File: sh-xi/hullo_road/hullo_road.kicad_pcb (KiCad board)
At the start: 2 copper layers, 70 x 43.5 mm, 139 parts

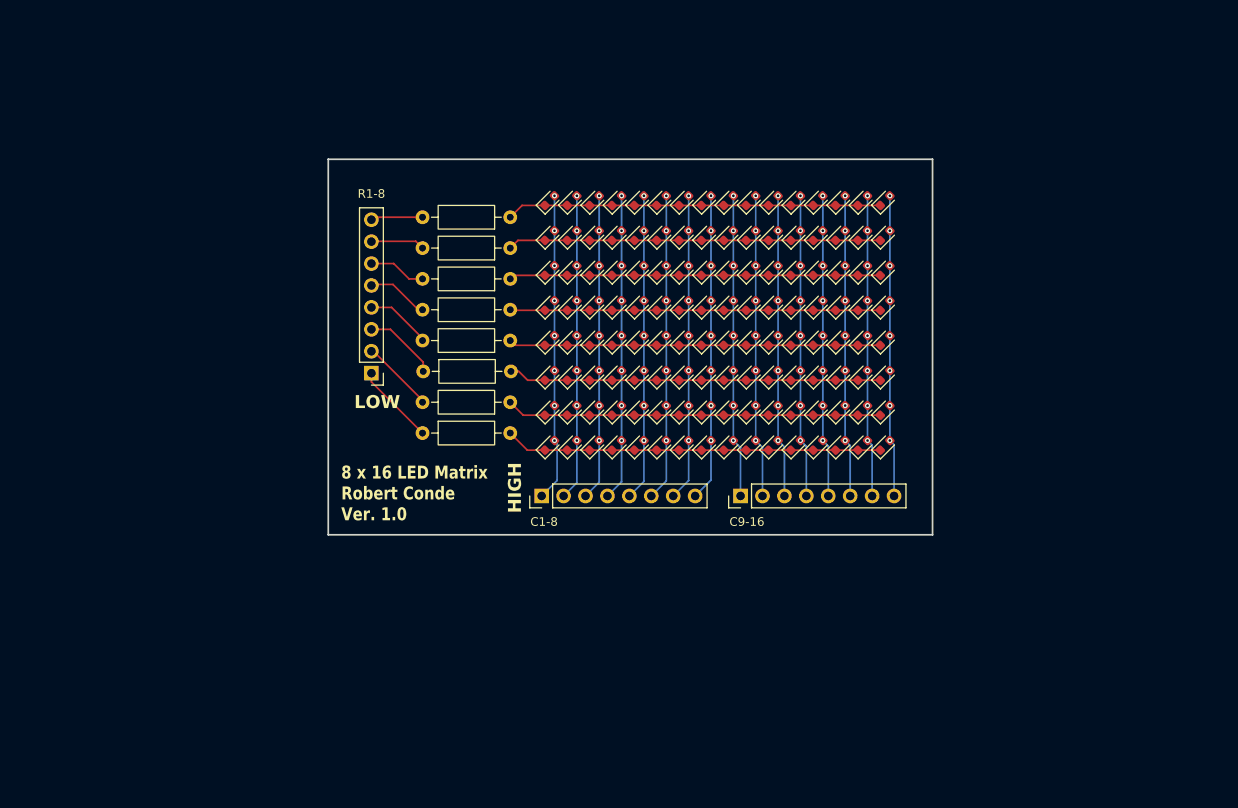
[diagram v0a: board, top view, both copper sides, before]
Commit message: Add LED matrix
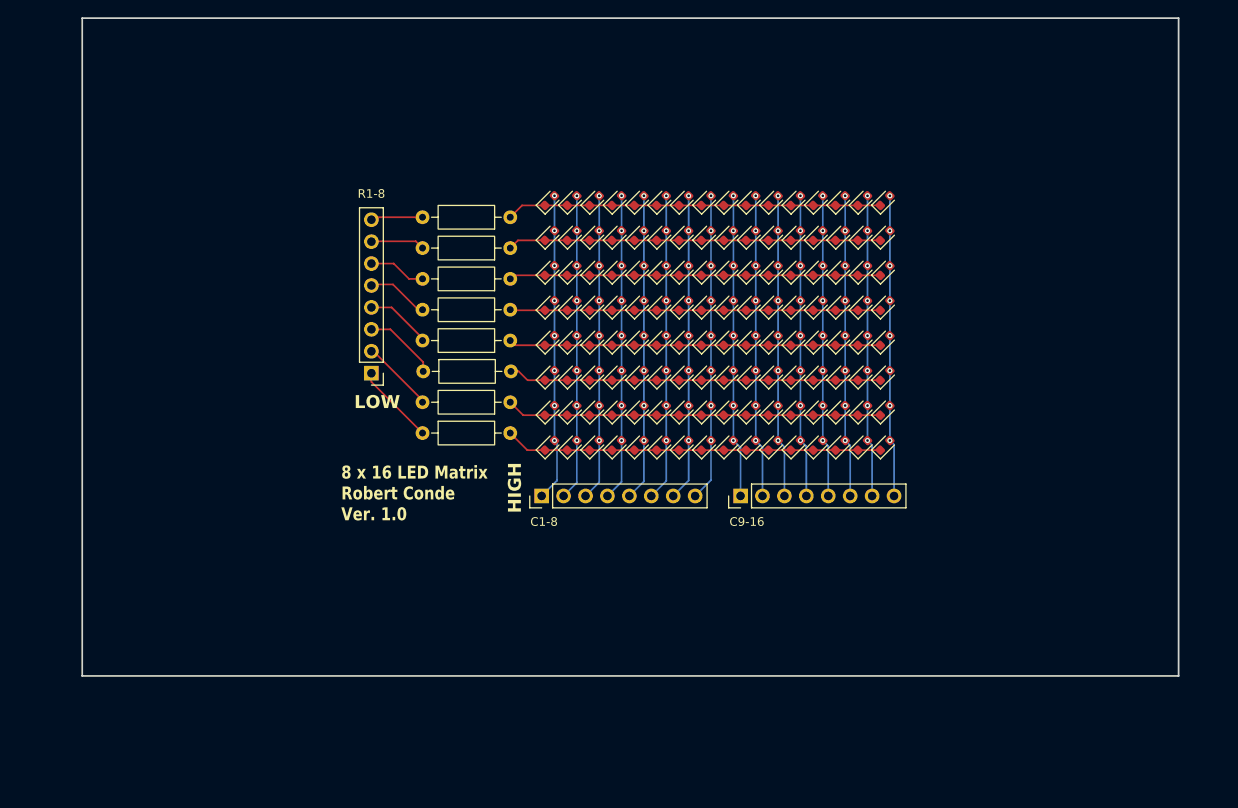
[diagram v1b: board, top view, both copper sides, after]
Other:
- board size 70 x 43.5 mm -> 127 x 76.2 mm
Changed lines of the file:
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@@
 	)
 	(gr_rect
-		(start 59.5 86)
-		(end 129.5 129.5)
+		(start 31 69.65)
+		(end 158 145.85)
 		(stroke
 			(width 0.2)
-			(type default)
+			(type solid)
 		)
 		(fill no)
+		(locked yes)
 		(layer "Edge.Cuts")
 	)

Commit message: Place LEDs in a grid
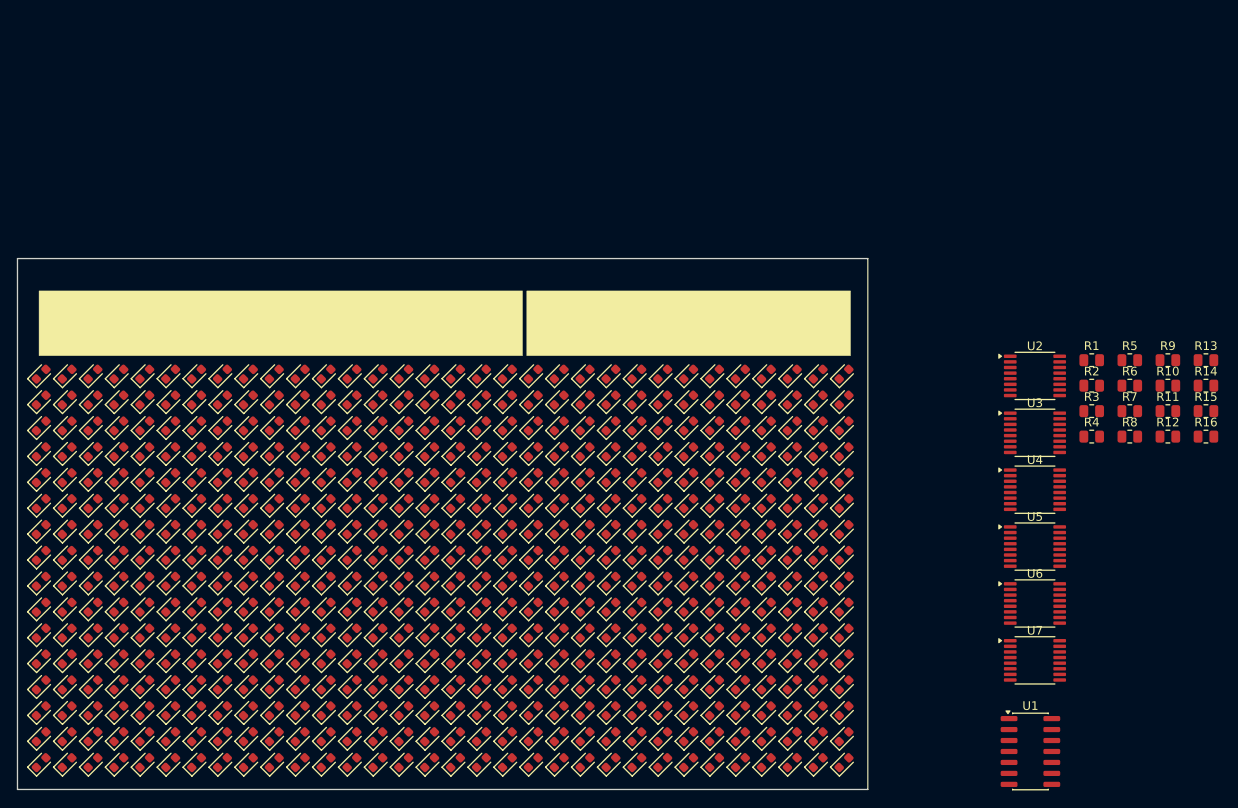
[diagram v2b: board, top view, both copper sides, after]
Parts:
- removed C1-8, C9-16, R1-8: Conn_01x08, Connector_PinHeader_2.54mm:PinHeader_1x08_P2.54mm_Vertical
- added D129: LED, LED_SMD:LED_0603_1608Metric, F.Cu at (26.2, 122.9)
- added D130: LED, LED_SMD:LED_0603_1608Metric, F.Cu at (29.2, 122.9)
- added D131: LED, LED_SMD:LED_0603_1608Metric, F.Cu at (32.2, 122.9)
- added D132: LED, LED_SMD:LED_0603_1608Metric, F.Cu at (35.2, 122.9)
- added D133: LED, LED_SMD:LED_0603_1608Metric, F.Cu at (38.2, 122.9)
- added D134: LED, LED_SMD:LED_0603_1608Metric, F.Cu at (41.2, 122.9)
- added D135: LED, LED_SMD:LED_0603_1608Metric, F.Cu at (44.2, 122.9)
- added D136: LED, LED_SMD:LED_0603_1608Metric, F.Cu at (47.2, 122.9)
- added D137: LED, LED_SMD:LED_0603_1608Metric, F.Cu at (50.2, 122.9)
- added D138: LED, LED_SMD:LED_0603_1608Metric, F.Cu at (53.2, 122.9)
- added D139: LED, LED_SMD:LED_0603_1608Metric, F.Cu at (56.2, 122.9)
- added D140: LED, LED_SMD:LED_0603_1608Metric, F.Cu at (59.2, 122.9)
- added D141: LED, LED_SMD:LED_0603_1608Metric, F.Cu at (62.2, 122.9)
- added D142: LED, LED_SMD:LED_0603_1608Metric, F.Cu at (65.2, 122.9)
- added D143: LED, LED_SMD:LED_0603_1608Metric, F.Cu at (68.2, 122.9)
- added D144: LED, LED_SMD:LED_0603_1608Metric, F.Cu at (71.2, 122.9)
- added D145: LED, LED_SMD:LED_0603_1608Metric, F.Cu at (74.2, 122.9)
- added D146: LED, LED_SMD:LED_0603_1608Metric, F.Cu at (77.2, 122.9)
- added D147: LED, LED_SMD:LED_0603_1608Metric, F.Cu at (80.2, 122.9)
- added D148: LED, LED_SMD:LED_0603_1608Metric, F.Cu at (83.2, 122.9)
- added D149: LED, LED_SMD:LED_0603_1608Metric, F.Cu at (86.2, 122.9)
- added D150: LED, LED_SMD:LED_0603_1608Metric, F.Cu at (89.2, 122.9)
- added D151: LED, LED_SMD:LED_0603_1608Metric, F.Cu at (92.2, 122.9)
- added D152: LED, LED_SMD:LED_0603_1608Metric, F.Cu at (95.2, 122.9)
- added D153: LED, LED_SMD:LED_0603_1608Metric, F.Cu at (98.2, 122.9)
- added D154: LED, LED_SMD:LED_0603_1608Metric, F.Cu at (101.2, 122.9)
- added D155: LED, LED_SMD:LED_0603_1608Metric, F.Cu at (104.2, 122.9)
- added D156: LED, LED_SMD:LED_0603_1608Metric, F.Cu at (107.2, 122.9)
- added D157: LED, LED_SMD:LED_0603_1608Metric, F.Cu at (110.2, 122.9)
- added D158: LED, LED_SMD:LED_0603_1608Metric, F.Cu at (113.2, 122.9)
- added D159: LED, LED_SMD:LED_0603_1608Metric, F.Cu at (116.2, 122.9)
- added D160: LED, LED_SMD:LED_0603_1608Metric, F.Cu at (119.2, 122.9)
- added D161: LED, LED_SMD:LED_0603_1608Metric, F.Cu at (26.2, 125.9)
- added D162: LED, LED_SMD:LED_0603_1608Metric, F.Cu at (29.2, 125.9)
- added D163: LED, LED_SMD:LED_0603_1608Metric, F.Cu at (32.2, 125.9)
- added D164: LED, LED_SMD:LED_0603_1608Metric, F.Cu at (35.2, 125.9)
- added D165: LED, LED_SMD:LED_0603_1608Metric, F.Cu at (38.2, 125.9)
- added D166: LED, LED_SMD:LED_0603_1608Metric, F.Cu at (41.2, 125.9)
- added D167: LED, LED_SMD:LED_0603_1608Metric, F.Cu at (44.2, 125.9)
- added D168: LED, LED_SMD:LED_0603_1608Metric, F.Cu at (47.2, 125.9)
- added D169: LED, LED_SMD:LED_0603_1608Metric, F.Cu at (50.2, 125.9)
- added D170: LED, LED_SMD:LED_0603_1608Metric, F.Cu at (53.2, 125.9)
- added D171: LED, LED_SMD:LED_0603_1608Metric, F.Cu at (56.2, 125.9)
- added D172: LED, LED_SMD:LED_0603_1608Metric, F.Cu at (59.2, 125.9)
- added D173: LED, LED_SMD:LED_0603_1608Metric, F.Cu at (62.2, 125.9)
- added D174: LED, LED_SMD:LED_0603_1608Metric, F.Cu at (65.2, 125.9)
- added D175: LED, LED_SMD:LED_0603_1608Metric, F.Cu at (68.2, 125.9)
- added D176: LED, LED_SMD:LED_0603_1608Metric, F.Cu at (71.2, 125.9)
- added D177: LED, LED_SMD:LED_0603_1608Metric, F.Cu at (74.2, 125.9)
- added D178: LED, LED_SMD:LED_0603_1608Metric, F.Cu at (77.2, 125.9)
- added D179: LED, LED_SMD:LED_0603_1608Metric, F.Cu at (80.2, 125.9)
- added D180: LED, LED_SMD:LED_0603_1608Metric, F.Cu at (83.2, 125.9)
- added D181: LED, LED_SMD:LED_0603_1608Metric, F.Cu at (86.2, 125.9)
- added D182: LED, LED_SMD:LED_0603_1608Metric, F.Cu at (89.2, 125.9)
- added D183: LED, LED_SMD:LED_0603_1608Metric, F.Cu at (92.2, 125.9)
- added D184: LED, LED_SMD:LED_0603_1608Metric, F.Cu at (95.2, 125.9)
- added D185: LED, LED_SMD:LED_0603_1608Metric, F.Cu at (98.2, 125.9)
- added D186: LED, LED_SMD:LED_0603_1608Metric, F.Cu at (101.2, 125.9)
- added D187: LED, LED_SMD:LED_0603_1608Metric, F.Cu at (104.2, 125.9)
- added D188: LED, LED_SMD:LED_0603_1608Metric, F.Cu at (107.2, 125.9)
- added D189: LED, LED_SMD:LED_0603_1608Metric, F.Cu at (110.2, 125.9)
- added D190: LED, LED_SMD:LED_0603_1608Metric, F.Cu at (113.2, 125.9)
- added D191: LED, LED_SMD:LED_0603_1608Metric, F.Cu at (116.2, 125.9)
- added D192: LED, LED_SMD:LED_0603_1608Metric, F.Cu at (119.2, 125.9)
- added D193: LED, LED_SMD:LED_0603_1608Metric, F.Cu at (26.2, 128.9)
- added D194: LED, LED_SMD:LED_0603_1608Metric, F.Cu at (29.2, 128.9)
- added D195: LED, LED_SMD:LED_0603_1608Metric, F.Cu at (32.2, 128.9)
- added D196: LED, LED_SMD:LED_0603_1608Metric, F.Cu at (35.2, 128.9)
- added D197: LED, LED_SMD:LED_0603_1608Metric, F.Cu at (38.2, 128.9)
- added D198: LED, LED_SMD:LED_0603_1608Metric, F.Cu at (41.2, 128.9)
- added D199: LED, LED_SMD:LED_0603_1608Metric, F.Cu at (44.2, 128.9)
- added D200: LED, LED_SMD:LED_0603_1608Metric, F.Cu at (47.2, 128.9)
- added D201: LED, LED_SMD:LED_0603_1608Metric, F.Cu at (50.2, 128.9)
- added D202: LED, LED_SMD:LED_0603_1608Metric, F.Cu at (53.2, 128.9)
- added D203: LED, LED_SMD:LED_0603_1608Metric, F.Cu at (56.2, 128.9)
- added D204: LED, LED_SMD:LED_0603_1608Metric, F.Cu at (59.2, 128.9)
- added D205: LED, LED_SMD:LED_0603_1608Metric, F.Cu at (62.2, 128.9)
- added D206: LED, LED_SMD:LED_0603_1608Metric, F.Cu at (65.2, 128.9)
- added D207: LED, LED_SMD:LED_0603_1608Metric, F.Cu at (68.2, 128.9)
- added D208: LED, LED_SMD:LED_0603_1608Metric, F.Cu at (71.2, 128.9)
- added D209: LED, LED_SMD:LED_0603_1608Metric, F.Cu at (74.2, 128.9)
- added D210: LED, LED_SMD:LED_0603_1608Metric, F.Cu at (77.2, 128.9)
- added D211: LED, LED_SMD:LED_0603_1608Metric, F.Cu at (80.2, 128.9)
- added D212: LED, LED_SMD:LED_0603_1608Metric, F.Cu at (83.2, 128.9)
- added D213: LED, LED_SMD:LED_0603_1608Metric, F.Cu at (86.2, 128.9)
- added D214: LED, LED_SMD:LED_0603_1608Metric, F.Cu at (89.2, 128.9)
- added D215: LED, LED_SMD:LED_0603_1608Metric, F.Cu at (92.2, 128.9)
- added D216: LED, LED_SMD:LED_0603_1608Metric, F.Cu at (95.2, 128.9)
- added D217: LED, LED_SMD:LED_0603_1608Metric, F.Cu at (98.2, 128.9)
- added D218: LED, LED_SMD:LED_0603_1608Metric, F.Cu at (101.2, 128.9)
- added D219: LED, LED_SMD:LED_0603_1608Metric, F.Cu at (104.2, 128.9)
- added D220: LED, LED_SMD:LED_0603_1608Metric, F.Cu at (107.2, 128.9)
- added D221: LED, LED_SMD:LED_0603_1608Metric, F.Cu at (110.2, 128.9)
- added D222: LED, LED_SMD:LED_0603_1608Metric, F.Cu at (113.2, 128.9)
- added D223: LED, LED_SMD:LED_0603_1608Metric, F.Cu at (116.2, 128.9)
- added D224: LED, LED_SMD:LED_0603_1608Metric, F.Cu at (119.2, 128.9)
- added D225: LED, LED_SMD:LED_0603_1608Metric, F.Cu at (26.2, 131.9)
- added D226: LED, LED_SMD:LED_0603_1608Metric, F.Cu at (29.2, 131.9)
- added D227: LED, LED_SMD:LED_0603_1608Metric, F.Cu at (32.2, 131.9)
- added D228: LED, LED_SMD:LED_0603_1608Metric, F.Cu at (35.2, 131.9)
- added D229: LED, LED_SMD:LED_0603_1608Metric, F.Cu at (38.2, 131.9)
- added D230: LED, LED_SMD:LED_0603_1608Metric, F.Cu at (41.2, 131.9)
- added D231: LED, LED_SMD:LED_0603_1608Metric, F.Cu at (44.2, 131.9)
- added D232: LED, LED_SMD:LED_0603_1608Metric, F.Cu at (47.2, 131.9)
- added D233: LED, LED_SMD:LED_0603_1608Metric, F.Cu at (50.2, 131.9)
- added D234: LED, LED_SMD:LED_0603_1608Metric, F.Cu at (53.2, 131.9)
- added D235: LED, LED_SMD:LED_0603_1608Metric, F.Cu at (56.2, 131.9)
- added D236: LED, LED_SMD:LED_0603_1608Metric, F.Cu at (59.2, 131.9)
- added D237: LED, LED_SMD:LED_0603_1608Metric, F.Cu at (62.2, 131.9)
- added D238: LED, LED_SMD:LED_0603_1608Metric, F.Cu at (65.2, 131.9)
- added D239: LED, LED_SMD:LED_0603_1608Metric, F.Cu at (68.2, 131.9)
- added D240: LED, LED_SMD:LED_0603_1608Metric, F.Cu at (71.2, 131.9)
- added D241: LED, LED_SMD:LED_0603_1608Metric, F.Cu at (74.2, 131.9)
- added D242: LED, LED_SMD:LED_0603_1608Metric, F.Cu at (77.2, 131.9)
- added D243: LED, LED_SMD:LED_0603_1608Metric, F.Cu at (80.2, 131.9)
- added D244: LED, LED_SMD:LED_0603_1608Metric, F.Cu at (83.2, 131.9)
- added D245: LED, LED_SMD:LED_0603_1608Metric, F.Cu at (86.2, 131.9)
- added D246: LED, LED_SMD:LED_0603_1608Metric, F.Cu at (89.2, 131.9)
- added D247: LED, LED_SMD:LED_0603_1608Metric, F.Cu at (92.2, 131.9)
- added D248: LED, LED_SMD:LED_0603_1608Metric, F.Cu at (95.2, 131.9)
- added D249: LED, LED_SMD:LED_0603_1608Metric, F.Cu at (98.2, 131.9)
- added D250: LED, LED_SMD:LED_0603_1608Metric, F.Cu at (101.2, 131.9)
- added D251: LED, LED_SMD:LED_0603_1608Metric, F.Cu at (104.2, 131.9)
- added D252: LED, LED_SMD:LED_0603_1608Metric, F.Cu at (107.2, 131.9)
- added D253: LED, LED_SMD:LED_0603_1608Metric, F.Cu at (110.2, 131.9)
- added D254: LED, LED_SMD:LED_0603_1608Metric, F.Cu at (113.2, 131.9)
- added D255: LED, LED_SMD:LED_0603_1608Metric, F.Cu at (116.2, 131.9)
- added D256: LED, LED_SMD:LED_0603_1608Metric, F.Cu at (119.2, 131.9)
- added D257: LED, LED_SMD:LED_0603_1608Metric, F.Cu at (26.2, 134.9)
- added D258: LED, LED_SMD:LED_0603_1608Metric, F.Cu at (29.2, 134.9)
- added D259: LED, LED_SMD:LED_0603_1608Metric, F.Cu at (32.2, 134.9)
- added D260: LED, LED_SMD:LED_0603_1608Metric, F.Cu at (35.2, 134.9)
- added D261: LED, LED_SMD:LED_0603_1608Metric, F.Cu at (38.2, 134.9)
- added D262: LED, LED_SMD:LED_0603_1608Metric, F.Cu at (41.2, 134.9)
- added D263: LED, LED_SMD:LED_0603_1608Metric, F.Cu at (44.2, 134.9)
- added D264: LED, LED_SMD:LED_0603_1608Metric, F.Cu at (47.2, 134.9)
- added D265: LED, LED_SMD:LED_0603_1608Metric, F.Cu at (50.2, 134.9)
- added D266: LED, LED_SMD:LED_0603_1608Metric, F.Cu at (53.2, 134.9)
- added D267: LED, LED_SMD:LED_0603_1608Metric, F.Cu at (56.2, 134.9)
- added D268: LED, LED_SMD:LED_0603_1608Metric, F.Cu at (59.2, 134.9)
- added D269: LED, LED_SMD:LED_0603_1608Metric, F.Cu at (62.2, 134.9)
- added D270: LED, LED_SMD:LED_0603_1608Metric, F.Cu at (65.2, 134.9)
- added D271: LED, LED_SMD:LED_0603_1608Metric, F.Cu at (68.2, 134.9)
- added D272: LED, LED_SMD:LED_0603_1608Metric, F.Cu at (71.2, 134.9)
- added D273: LED, LED_SMD:LED_0603_1608Metric, F.Cu at (74.2, 134.9)
- added D274: LED, LED_SMD:LED_0603_1608Metric, F.Cu at (77.2, 134.9)
- added D275: LED, LED_SMD:LED_0603_1608Metric, F.Cu at (80.2, 134.9)
- added D276: LED, LED_SMD:LED_0603_1608Metric, F.Cu at (83.2, 134.9)
- added D277: LED, LED_SMD:LED_0603_1608Metric, F.Cu at (86.2, 134.9)
- added D278: LED, LED_SMD:LED_0603_1608Metric, F.Cu at (89.2, 134.9)
- added D279: LED, LED_SMD:LED_0603_1608Metric, F.Cu at (92.2, 134.9)
- added D280: LED, LED_SMD:LED_0603_1608Metric, F.Cu at (95.2, 134.9)
- added D281: LED, LED_SMD:LED_0603_1608Metric, F.Cu at (98.2, 134.9)
- added D282: LED, LED_SMD:LED_0603_1608Metric, F.Cu at (101.2, 134.9)
- added D283: LED, LED_SMD:LED_0603_1608Metric, F.Cu at (104.2, 134.9)
- added D284: LED, LED_SMD:LED_0603_1608Metric, F.Cu at (107.2, 134.9)
- added D285: LED, LED_SMD:LED_0603_1608Metric, F.Cu at (110.2, 134.9)
- added D286: LED, LED_SMD:LED_0603_1608Metric, F.Cu at (113.2, 134.9)
- added D287: LED, LED_SMD:LED_0603_1608Metric, F.Cu at (116.2, 134.9)
- added D288: LED, LED_SMD:LED_0603_1608Metric, F.Cu at (119.2, 134.9)
- added D289: LED, LED_SMD:LED_0603_1608Metric, F.Cu at (26.2, 137.9)
- added D290: LED, LED_SMD:LED_0603_1608Metric, F.Cu at (29.2, 137.9)
- added D291: LED, LED_SMD:LED_0603_1608Metric, F.Cu at (32.2, 137.9)
- added D292: LED, LED_SMD:LED_0603_1608Metric, F.Cu at (35.2, 137.9)
- added D293: LED, LED_SMD:LED_0603_1608Metric, F.Cu at (38.2, 137.9)
- added D294: LED, LED_SMD:LED_0603_1608Metric, F.Cu at (41.2, 137.9)
- added D295: LED, LED_SMD:LED_0603_1608Metric, F.Cu at (44.2, 137.9)
- added D296: LED, LED_SMD:LED_0603_1608Metric, F.Cu at (47.2, 137.9)
- added D297: LED, LED_SMD:LED_0603_1608Metric, F.Cu at (50.2, 137.9)
- added D298: LED, LED_SMD:LED_0603_1608Metric, F.Cu at (53.2, 137.9)
- added D299: LED, LED_SMD:LED_0603_1608Metric, F.Cu at (56.2, 137.9)
- added D300: LED, LED_SMD:LED_0603_1608Metric, F.Cu at (59.2, 137.9)
- added D301: LED, LED_SMD:LED_0603_1608Metric, F.Cu at (62.2, 137.9)
- added D302: LED, LED_SMD:LED_0603_1608Metric, F.Cu at (65.2, 137.9)
- added D303: LED, LED_SMD:LED_0603_1608Metric, F.Cu at (68.2, 137.9)
- added D304: LED, LED_SMD:LED_0603_1608Metric, F.Cu at (71.2, 137.9)
- added D305: LED, LED_SMD:LED_0603_1608Metric, F.Cu at (74.2, 137.9)
- added D306: LED, LED_SMD:LED_0603_1608Metric, F.Cu at (77.2, 137.9)
- added D307: LED, LED_SMD:LED_0603_1608Metric, F.Cu at (80.2, 137.9)
- added D308: LED, LED_SMD:LED_0603_1608Metric, F.Cu at (83.2, 137.9)
- added D309: LED, LED_SMD:LED_0603_1608Metric, F.Cu at (86.2, 137.9)
- added D310: LED, LED_SMD:LED_0603_1608Metric, F.Cu at (89.2, 137.9)
- added D311: LED, LED_SMD:LED_0603_1608Metric, F.Cu at (92.2, 137.9)
- added D312: LED, LED_SMD:LED_0603_1608Metric, F.Cu at (95.2, 137.9)
- added D313: LED, LED_SMD:LED_0603_1608Metric, F.Cu at (98.2, 137.9)
- added D314: LED, LED_SMD:LED_0603_1608Metric, F.Cu at (101.2, 137.9)
- added D315: LED, LED_SMD:LED_0603_1608Metric, F.Cu at (104.2, 137.9)
- added D316: LED, LED_SMD:LED_0603_1608Metric, F.Cu at (107.2, 137.9)
- added D317: LED, LED_SMD:LED_0603_1608Metric, F.Cu at (110.2, 137.9)
- added D318: LED, LED_SMD:LED_0603_1608Metric, F.Cu at (113.2, 137.9)
- added D319: LED, LED_SMD:LED_0603_1608Metric, F.Cu at (116.2, 137.9)
- added D320: LED, LED_SMD:LED_0603_1608Metric, F.Cu at (119.2, 137.9)
- added D321: LED, LED_SMD:LED_0603_1608Metric, F.Cu at (26.2, 140.9)
- added D322: LED, LED_SMD:LED_0603_1608Metric, F.Cu at (29.2, 140.9)
- added D323: LED, LED_SMD:LED_0603_1608Metric, F.Cu at (32.2, 140.9)
- added D324: LED, LED_SMD:LED_0603_1608Metric, F.Cu at (35.2, 140.9)
- added D325: LED, LED_SMD:LED_0603_1608Metric, F.Cu at (38.2, 140.9)
- added D326: LED, LED_SMD:LED_0603_1608Metric, F.Cu at (41.2, 140.9)
- added D327: LED, LED_SMD:LED_0603_1608Metric, F.Cu at (44.2, 140.9)
- added D328: LED, LED_SMD:LED_0603_1608Metric, F.Cu at (47.2, 140.9)
- added D329: LED, LED_SMD:LED_0603_1608Metric, F.Cu at (50.2, 140.9)
- added D330: LED, LED_SMD:LED_0603_1608Metric, F.Cu at (53.2, 140.9)
- added D331: LED, LED_SMD:LED_0603_1608Metric, F.Cu at (56.2, 140.9)
- added D332: LED, LED_SMD:LED_0603_1608Metric, F.Cu at (59.2, 140.9)
- added D333: LED, LED_SMD:LED_0603_1608Metric, F.Cu at (62.2, 140.9)
- added D334: LED, LED_SMD:LED_0603_1608Metric, F.Cu at (65.2, 140.9)
- added D335: LED, LED_SMD:LED_0603_1608Metric, F.Cu at (68.2, 140.9)
- added D336: LED, LED_SMD:LED_0603_1608Metric, F.Cu at (71.2, 140.9)
- added D337: LED, LED_SMD:LED_0603_1608Metric, F.Cu at (74.2, 140.9)
- added D338: LED, LED_SMD:LED_0603_1608Metric, F.Cu at (77.2, 140.9)
- added D339: LED, LED_SMD:LED_0603_1608Metric, F.Cu at (80.2, 140.9)
- added D340: LED, LED_SMD:LED_0603_1608Metric, F.Cu at (83.2, 140.9)
- added D341: LED, LED_SMD:LED_0603_1608Metric, F.Cu at (86.2, 140.9)
- added D342: LED, LED_SMD:LED_0603_1608Metric, F.Cu at (89.2, 140.9)
- added D343: LED, LED_SMD:LED_0603_1608Metric, F.Cu at (92.2, 140.9)
- added D344: LED, LED_SMD:LED_0603_1608Metric, F.Cu at (95.2, 140.9)
- added D345: LED, LED_SMD:LED_0603_1608Metric, F.Cu at (98.2, 140.9)
- added D346: LED, LED_SMD:LED_0603_1608Metric, F.Cu at (101.2, 140.9)
- added D347: LED, LED_SMD:LED_0603_1608Metric, F.Cu at (104.2, 140.9)
- added D348: LED, LED_SMD:LED_0603_1608Metric, F.Cu at (107.2, 140.9)
- added D349: LED, LED_SMD:LED_0603_1608Metric, F.Cu at (110.2, 140.9)
- added D350: LED, LED_SMD:LED_0603_1608Metric, F.Cu at (113.2, 140.9)
- added D351: LED, LED_SMD:LED_0603_1608Metric, F.Cu at (116.2, 140.9)
- added D352: LED, LED_SMD:LED_0603_1608Metric, F.Cu at (119.2, 140.9)
- added D353: LED, LED_SMD:LED_0603_1608Metric, F.Cu at (26.2, 143.9)
- added D354: LED, LED_SMD:LED_0603_1608Metric, F.Cu at (29.2, 143.9)
- added D355: LED, LED_SMD:LED_0603_1608Metric, F.Cu at (32.2, 143.9)
- added D356: LED, LED_SMD:LED_0603_1608Metric, F.Cu at (35.2, 143.9)
- added D357: LED, LED_SMD:LED_0603_1608Metric, F.Cu at (38.2, 143.9)
- added D358: LED, LED_SMD:LED_0603_1608Metric, F.Cu at (41.2, 143.9)
- added D359: LED, LED_SMD:LED_0603_1608Metric, F.Cu at (44.2, 143.9)
- added D360: LED, LED_SMD:LED_0603_1608Metric, F.Cu at (47.2, 143.9)
- added D361: LED, LED_SMD:LED_0603_1608Metric, F.Cu at (50.2, 143.9)
- added D362: LED, LED_SMD:LED_0603_1608Metric, F.Cu at (53.2, 143.9)
- added D363: LED, LED_SMD:LED_0603_1608Metric, F.Cu at (56.2, 143.9)
- added D364: LED, LED_SMD:LED_0603_1608Metric, F.Cu at (59.2, 143.9)
- added D365: LED, LED_SMD:LED_0603_1608Metric, F.Cu at (62.2, 143.9)
- added D366: LED, LED_SMD:LED_0603_1608Metric, F.Cu at (65.2, 143.9)
- added D367: LED, LED_SMD:LED_0603_1608Metric, F.Cu at (68.2, 143.9)
- added D368: LED, LED_SMD:LED_0603_1608Metric, F.Cu at (71.2, 143.9)
- added D369: LED, LED_SMD:LED_0603_1608Metric, F.Cu at (74.2, 143.9)
- added D370: LED, LED_SMD:LED_0603_1608Metric, F.Cu at (77.2, 143.9)
- added D371: LED, LED_SMD:LED_0603_1608Metric, F.Cu at (80.2, 143.9)
- added D372: LED, LED_SMD:LED_0603_1608Metric, F.Cu at (83.2, 143.9)
- added D373: LED, LED_SMD:LED_0603_1608Metric, F.Cu at (86.2, 143.9)
- added D374: LED, LED_SMD:LED_0603_1608Metric, F.Cu at (89.2, 143.9)
- added D375: LED, LED_SMD:LED_0603_1608Metric, F.Cu at (92.2, 143.9)
- added D376: LED, LED_SMD:LED_0603_1608Metric, F.Cu at (95.2, 143.9)
- added D377: LED, LED_SMD:LED_0603_1608Metric, F.Cu at (98.2, 143.9)
- added D378: LED, LED_SMD:LED_0603_1608Metric, F.Cu at (101.2, 143.9)
- added D379: LED, LED_SMD:LED_0603_1608Metric, F.Cu at (104.2, 143.9)
- added D380: LED, LED_SMD:LED_0603_1608Metric, F.Cu at (107.2, 143.9)
- added D381: LED, LED_SMD:LED_0603_1608Metric, F.Cu at (110.2, 143.9)
- added D382: LED, LED_SMD:LED_0603_1608Metric, F.Cu at (113.2, 143.9)
- added D383: LED, LED_SMD:LED_0603_1608Metric, F.Cu at (116.2, 143.9)
- added D384: LED, LED_SMD:LED_0603_1608Metric, F.Cu at (119.2, 143.9)
- added D385: LED, LED_SMD:LED_0603_1608Metric, F.Cu at (26.2, 146.9)
- added D386: LED, LED_SMD:LED_0603_1608Metric, F.Cu at (29.2, 146.9)
- added D387: LED, LED_SMD:LED_0603_1608Metric, F.Cu at (32.2, 146.9)
- added D388: LED, LED_SMD:LED_0603_1608Metric, F.Cu at (35.2, 146.9)
- added D389: LED, LED_SMD:LED_0603_1608Metric, F.Cu at (38.2, 146.9)
- added D390: LED, LED_SMD:LED_0603_1608Metric, F.Cu at (41.2, 146.9)
- added D391: LED, LED_SMD:LED_0603_1608Metric, F.Cu at (44.2, 146.9)
- added D392: LED, LED_SMD:LED_0603_1608Metric, F.Cu at (47.2, 146.9)
- added D393: LED, LED_SMD:LED_0603_1608Metric, F.Cu at (50.2, 146.9)
- added D394: LED, LED_SMD:LED_0603_1608Metric, F.Cu at (53.2, 146.9)
- added D395: LED, LED_SMD:LED_0603_1608Metric, F.Cu at (56.2, 146.9)
- added D396: LED, LED_SMD:LED_0603_1608Metric, F.Cu at (59.2, 146.9)
- added D397: LED, LED_SMD:LED_0603_1608Metric, F.Cu at (62.2, 146.9)
- added D398: LED, LED_SMD:LED_0603_1608Metric, F.Cu at (65.2, 146.9)
- added D399: LED, LED_SMD:LED_0603_1608Metric, F.Cu at (68.2, 146.9)
- added D400: LED, LED_SMD:LED_0603_1608Metric, F.Cu at (71.2, 146.9)
- added D401: LED, LED_SMD:LED_0603_1608Metric, F.Cu at (74.2, 146.9)
- added D402: LED, LED_SMD:LED_0603_1608Metric, F.Cu at (77.2, 146.9)
- added D403: LED, LED_SMD:LED_0603_1608Metric, F.Cu at (80.2, 146.9)
- added D404: LED, LED_SMD:LED_0603_1608Metric, F.Cu at (83.2, 146.9)
- added D405: LED, LED_SMD:LED_0603_1608Metric, F.Cu at (86.2, 146.9)
- added D406: LED, LED_SMD:LED_0603_1608Metric, F.Cu at (89.2, 146.9)
- added D407: LED, LED_SMD:LED_0603_1608Metric, F.Cu at (92.2, 146.9)
- added D408: LED, LED_SMD:LED_0603_1608Metric, F.Cu at (95.2, 146.9)
- added D409: LED, LED_SMD:LED_0603_1608Metric, F.Cu at (98.2, 146.9)
- added D410: LED, LED_SMD:LED_0603_1608Metric, F.Cu at (101.2, 146.9)
- added D411: LED, LED_SMD:LED_0603_1608Metric, F.Cu at (104.2, 146.9)
- added D412: LED, LED_SMD:LED_0603_1608Metric, F.Cu at (107.2, 146.9)
- added D413: LED, LED_SMD:LED_0603_1608Metric, F.Cu at (110.2, 146.9)
- added D414: LED, LED_SMD:LED_0603_1608Metric, F.Cu at (113.2, 146.9)
- added D415: LED, LED_SMD:LED_0603_1608Metric, F.Cu at (116.2, 146.9)
- added D416: LED, LED_SMD:LED_0603_1608Metric, F.Cu at (119.2, 146.9)
- added D417: LED, LED_SMD:LED_0603_1608Metric, F.Cu at (26.2, 149.9)
- added D418: LED, LED_SMD:LED_0603_1608Metric, F.Cu at (29.2, 149.9)
- added D419: LED, LED_SMD:LED_0603_1608Metric, F.Cu at (32.2, 149.9)
- added D420: LED, LED_SMD:LED_0603_1608Metric, F.Cu at (35.2, 149.9)
- added D421: LED, LED_SMD:LED_0603_1608Metric, F.Cu at (38.2, 149.9)
- added D422: LED, LED_SMD:LED_0603_1608Metric, F.Cu at (41.2, 149.9)
- added D423: LED, LED_SMD:LED_0603_1608Metric, F.Cu at (44.2, 149.9)
- added D424: LED, LED_SMD:LED_0603_1608Metric, F.Cu at (47.2, 149.9)
- added D425: LED, LED_SMD:LED_0603_1608Metric, F.Cu at (50.2, 149.9)
- added D426: LED, LED_SMD:LED_0603_1608Metric, F.Cu at (53.2, 149.9)
- added D427: LED, LED_SMD:LED_0603_1608Metric, F.Cu at (56.2, 149.9)
- added D428: LED, LED_SMD:LED_0603_1608Metric, F.Cu at (59.2, 149.9)
- added D429: LED, LED_SMD:LED_0603_1608Metric, F.Cu at (62.2, 149.9)
- added D430: LED, LED_SMD:LED_0603_1608Metric, F.Cu at (65.2, 149.9)
- added D431: LED, LED_SMD:LED_0603_1608Metric, F.Cu at (68.2, 149.9)
- added D432: LED, LED_SMD:LED_0603_1608Metric, F.Cu at (71.2, 149.9)
- added D433: LED, LED_SMD:LED_0603_1608Metric, F.Cu at (74.2, 149.9)
- added D434: LED, LED_SMD:LED_0603_1608Metric, F.Cu at (77.2, 149.9)
- added D435: LED, LED_SMD:LED_0603_1608Metric, F.Cu at (80.2, 149.9)
- added D436: LED, LED_SMD:LED_0603_1608Metric, F.Cu at (83.2, 149.9)
- added D437: LED, LED_SMD:LED_0603_1608Metric, F.Cu at (86.2, 149.9)
- added D438: LED, LED_SMD:LED_0603_1608Metric, F.Cu at (89.2, 149.9)
- added D439: LED, LED_SMD:LED_0603_1608Metric, F.Cu at (92.2, 149.9)
- added D440: LED, LED_SMD:LED_0603_1608Metric, F.Cu at (95.2, 149.9)
- added D441: LED, LED_SMD:LED_0603_1608Metric, F.Cu at (98.2, 149.9)
- added D442: LED, LED_SMD:LED_0603_1608Metric, F.Cu at (101.2, 149.9)
- added D443: LED, LED_SMD:LED_0603_1608Metric, F.Cu at (104.2, 149.9)
- added D444: LED, LED_SMD:LED_0603_1608Metric, F.Cu at (107.2, 149.9)
- added D445: LED, LED_SMD:LED_0603_1608Metric, F.Cu at (110.2, 149.9)
- added D446: LED, LED_SMD:LED_0603_1608Metric, F.Cu at (113.2, 149.9)
- added D447: LED, LED_SMD:LED_0603_1608Metric, F.Cu at (116.2, 149.9)
- added D448: LED, LED_SMD:LED_0603_1608Metric, F.Cu at (119.2, 149.9)
- added D449: LED, LED_SMD:LED_0603_1608Metric, F.Cu at (26.2, 152.9)
- added D450: LED, LED_SMD:LED_0603_1608Metric, F.Cu at (29.2, 152.9)
- added D451: LED, LED_SMD:LED_0603_1608Metric, F.Cu at (32.2, 152.9)
- added D452: LED, LED_SMD:LED_0603_1608Metric, F.Cu at (35.2, 152.9)
- added D453: LED, LED_SMD:LED_0603_1608Metric, F.Cu at (38.2, 152.9)
- added D454: LED, LED_SMD:LED_0603_1608Metric, F.Cu at (41.2, 152.9)
- added D455: LED, LED_SMD:LED_0603_1608Metric, F.Cu at (44.2, 152.9)
- added D456: LED, LED_SMD:LED_0603_1608Metric, F.Cu at (47.2, 152.9)
- added D457: LED, LED_SMD:LED_0603_1608Metric, F.Cu at (50.2, 152.9)
- added D458: LED, LED_SMD:LED_0603_1608Metric, F.Cu at (53.2, 152.9)
- added D459: LED, LED_SMD:LED_0603_1608Metric, F.Cu at (56.2, 152.9)
- added D460: LED, LED_SMD:LED_0603_1608Metric, F.Cu at (59.2, 152.9)
- added D461: LED, LED_SMD:LED_0603_1608Metric, F.Cu at (62.2, 152.9)
- added D462: LED, LED_SMD:LED_0603_1608Metric, F.Cu at (65.2, 152.9)
- added D463: LED, LED_SMD:LED_0603_1608Metric, F.Cu at (68.2, 152.9)
- added D464: LED, LED_SMD:LED_0603_1608Metric, F.Cu at (71.2, 152.9)
- added D465: LED, LED_SMD:LED_0603_1608Metric, F.Cu at (74.2, 152.9)
- added D466: LED, LED_SMD:LED_0603_1608Metric, F.Cu at (77.2, 152.9)
- added D467: LED, LED_SMD:LED_0603_1608Metric, F.Cu at (80.2, 152.9)
- added D468: LED, LED_SMD:LED_0603_1608Metric, F.Cu at (83.2, 152.9)
- added D469: LED, LED_SMD:LED_0603_1608Metric, F.Cu at (86.2, 152.9)
- added D470: LED, LED_SMD:LED_0603_1608Metric, F.Cu at (89.2, 152.9)
- added D471: LED, LED_SMD:LED_0603_1608Metric, F.Cu at (92.2, 152.9)
- added D472: LED, LED_SMD:LED_0603_1608Metric, F.Cu at (95.2, 152.9)
- added D473: LED, LED_SMD:LED_0603_1608Metric, F.Cu at (98.2, 152.9)
- added D474: LED, LED_SMD:LED_0603_1608Metric, F.Cu at (101.2, 152.9)
- added D475: LED, LED_SMD:LED_0603_1608Metric, F.Cu at (104.2, 152.9)
- added D476: LED, LED_SMD:LED_0603_1608Metric, F.Cu at (107.2, 152.9)
- added D477: LED, LED_SMD:LED_0603_1608Metric, F.Cu at (110.2, 152.9)
- added D478: LED, LED_SMD:LED_0603_1608Metric, F.Cu at (113.2, 152.9)
- added D479: LED, LED_SMD:LED_0603_1608Metric, F.Cu at (116.2, 152.9)
- added D480: LED, LED_SMD:LED_0603_1608Metric, F.Cu at (119.2, 152.9)
- added D481: LED, LED_SMD:LED_0603_1608Metric, F.Cu at (26.2, 155.9)
- added D482: LED, LED_SMD:LED_0603_1608Metric, F.Cu at (29.2, 155.9)
- added D483: LED, LED_SMD:LED_0603_1608Metric, F.Cu at (32.2, 155.9)
- added D484: LED, LED_SMD:LED_0603_1608Metric, F.Cu at (35.2, 155.9)
- added D485: LED, LED_SMD:LED_0603_1608Metric, F.Cu at (38.2, 155.9)
- added D486: LED, LED_SMD:LED_0603_1608Metric, F.Cu at (41.2, 155.9)
- added D487: LED, LED_SMD:LED_0603_1608Metric, F.Cu at (44.2, 155.9)
- added D488: LED, LED_SMD:LED_0603_1608Metric, F.Cu at (47.2, 155.9)
- added D489: LED, LED_SMD:LED_0603_1608Metric, F.Cu at (50.2, 155.9)
- added D490: LED, LED_SMD:LED_0603_1608Metric, F.Cu at (53.2, 155.9)
- added D491: LED, LED_SMD:LED_0603_1608Metric, F.Cu at (56.2, 155.9)
- added D492: LED, LED_SMD:LED_0603_1608Metric, F.Cu at (59.2, 155.9)
- added D493: LED, LED_SMD:LED_0603_1608Metric, F.Cu at (62.2, 155.9)
- added D494: LED, LED_SMD:LED_0603_1608Metric, F.Cu at (65.2, 155.9)
- added D495: LED, LED_SMD:LED_0603_1608Metric, F.Cu at (68.2, 155.9)
- added D496: LED, LED_SMD:LED_0603_1608Metric, F.Cu at (71.2, 155.9)
- added D497: LED, LED_SMD:LED_0603_1608Metric, F.Cu at (74.2, 155.9)
- added D498: LED, LED_SMD:LED_0603_1608Metric, F.Cu at (77.2, 155.9)
- added D499: LED, LED_SMD:LED_0603_1608Metric, F.Cu at (80.2, 155.9)
- added D500: LED, LED_SMD:LED_0603_1608Metric, F.Cu at (83.2, 155.9)
- added D501: LED, LED_SMD:LED_0603_1608Metric, F.Cu at (86.2, 155.9)
- added D502: LED, LED_SMD:LED_0603_1608Metric, F.Cu at (89.2, 155.9)
- added D503: LED, LED_SMD:LED_0603_1608Metric, F.Cu at (92.2, 155.9)
- added D504: LED, LED_SMD:LED_0603_1608Metric, F.Cu at (95.2, 155.9)
- added D505: LED, LED_SMD:LED_0603_1608Metric, F.Cu at (98.2, 155.9)
- added D506: LED, LED_SMD:LED_0603_1608Metric, F.Cu at (101.2, 155.9)
- added D507: LED, LED_SMD:LED_0603_1608Metric, F.Cu at (104.2, 155.9)
- added D508: LED, LED_SMD:LED_0603_1608Metric, F.Cu at (107.2, 155.9)
- added D509: LED, LED_SMD:LED_0603_1608Metric, F.Cu at (110.2, 155.9)
- added D510: LED, LED_SMD:LED_0603_1608Metric, F.Cu at (113.2, 155.9)
- added D511: LED, LED_SMD:LED_0603_1608Metric, F.Cu at (116.2, 155.9)
- added D512: LED, LED_SMD:LED_0603_1608Metric, F.Cu at (119.2, 155.9)
- added R10: 10R, Resistor_SMD:R_0805_2012Metric, F.Cu at (156.8, 112.2)
- added R11: 10R, Resistor_SMD:R_0805_2012Metric, F.Cu at (156.8, 115.2)
- added R12: 10R, Resistor_SMD:R_0805_2012Metric, F.Cu at (156.8, 118.1)
- added R13: 10R, Resistor_SMD:R_0805_2012Metric, F.Cu at (161.2, 109.3)
- added R14: 10R, Resistor_SMD:R_0805_2012Metric, F.Cu at (161.2, 112.2)
- added R15: 10R, Resistor_SMD:R_0805_2012Metric, F.Cu at (161.2, 115.2)
- added R16: 10R, Resistor_SMD:R_0805_2012Metric, F.Cu at (161.2, 118.1)
- added R9: 10R, Resistor_SMD:R_0805_2012Metric, F.Cu at (156.8, 109.3)
- added U1: ATtiny414-SS, Package_SO:SOIC-14_3.9x8.7mm_P1.27mm, F.Cu at (140.8, 154.6)
- added U2: 74HC595, Package_SO:TSSOP-16_4.4x5mm_P0.65mm, F.Cu at (141.4, 111.1)
- added U3: 74HC595, Package_SO:TSSOP-16_4.4x5mm_P0.65mm, F.Cu at (141.4, 117.7)
- added U4: 74HC595, Package_SO:TSSOP-16_4.4x5mm_P0.65mm, F.Cu at (141.4, 124.3)
- added U5: 74HC595, Package_SO:TSSOP-16_4.4x5mm_P0.65mm, F.Cu at (141.4, 130.9)
- added U6: 74HC595, Package_SO:TSSOP-16_4.4x5mm_P0.65mm, F.Cu at (141.4, 137.5)
- added U7: 74HC595, Package_SO:TSSOP-16_4.4x5mm_P0.65mm, F.Cu at (141.4, 144.0)
- R1, R2, R3, R4, R5, R6, R7, R8: value 110 -> 10R; footprint Resistor_THT:R_Axial_DIN0207_L6.3mm_D2.5mm_P10.16mm_Horizontal -> Resistor_SMD:R_0805_2012Metric
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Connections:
- D1 pad 1: Net-(D1-K) -> Row0
- D1 pad 2: Net-(C1-8-Pin_1) -> Col0
- D10 pad 1: Net-(D1-K) -> Row0
- D10 pad 2: Net-(C9-16-Pin_2) -> Col9
- D100 pad 1: Net-(D100-K) -> Row3
- D100 pad 2: Net-(C1-8-Pin_4) -> Col3
- D101 pad 1: Net-(D100-K) -> Row3
- D101 pad 2: Net-(C1-8-Pin_5) -> Col4
- D102 pad 1: Net-(D100-K) -> Row3
- D102 pad 2: Net-(C1-8-Pin_6) -> Col5
- D103 pad 1: Net-(D100-K) -> Row3
- D103 pad 2: Net-(C1-8-Pin_7) -> Col6
- D104 pad 1: Net-(D100-K) -> Row3
- D104 pad 2: Net-(C1-8-Pin_8) -> Col7
- D105 pad 1: Net-(D100-K) -> Row3
- D105 pad 2: Net-(C9-16-Pin_1) -> Col8
- D106 pad 1: Net-(D100-K) -> Row3
- D106 pad 2: Net-(C9-16-Pin_2) -> Col9
- D107 pad 1: Net-(D100-K) -> Row3
- D107 pad 2: Net-(C9-16-Pin_3) -> Col10
- D108 pad 1: Net-(D100-K) -> Row3
- D108 pad 2: Net-(C9-16-Pin_4) -> Col11
- D109 pad 1: Net-(D100-K) -> Row3
- D109 pad 2: Net-(C9-16-Pin_5) -> Col12
- D11 pad 1: Net-(D1-K) -> Row0
- D11 pad 2: Net-(C9-16-Pin_3) -> Col10
- D110 pad 1: Net-(D100-K) -> Row3
- D110 pad 2: Net-(C9-16-Pin_6) -> Col13
- D111 pad 1: Net-(D100-K) -> Row3
- D111 pad 2: Net-(C9-16-Pin_7) -> Col14
- D112 pad 1: Net-(D100-K) -> Row3
- D112 pad 2: Net-(C9-16-Pin_8) -> Col15
- D113 pad 1: Net-(D113-K) -> Row3
- D113 pad 2: Net-(C1-8-Pin_1) -> Col16
- D114 pad 1: Net-(D113-K) -> Row3
- D114 pad 2: Net-(C1-8-Pin_2) -> Col17
- D115 pad 1: Net-(D113-K) -> Row3
- D115 pad 2: Net-(C1-8-Pin_3) -> Col18
- D116 pad 1: Net-(D113-K) -> Row3
- D116 pad 2: Net-(C1-8-Pin_4) -> Col19
- D117 pad 1: Net-(D113-K) -> Row3
- D117 pad 2: Net-(C1-8-Pin_5) -> Col20
- D118 pad 1: Net-(D113-K) -> Row3
- D118 pad 2: Net-(C1-8-Pin_6) -> Col21
- D119 pad 1: Net-(D113-K) -> Row3
- D119 pad 2: Net-(C1-8-Pin_7) -> Col22
- D12 pad 1: Net-(D1-K) -> Row0
- D12 pad 2: Net-(C9-16-Pin_4) -> Col11
- D120 pad 1: Net-(D113-K) -> Row3
- D120 pad 2: Net-(C1-8-Pin_8) -> Col23
- D121 pad 1: Net-(D113-K) -> Row3
- D121 pad 2: Net-(C9-16-Pin_1) -> Col24
- D122 pad 1: Net-(D113-K) -> Row3
- D122 pad 2: Net-(C9-16-Pin_2) -> Col25
- D123 pad 1: Net-(D113-K) -> Row3
- D123 pad 2: Net-(C9-16-Pin_3) -> Col26
- D124 pad 1: Net-(D113-K) -> Row3
- D124 pad 2: Net-(C9-16-Pin_4) -> Col27
- D125 pad 1: Net-(D113-K) -> Row3
- D125 pad 2: Net-(C9-16-Pin_5) -> Col28
- D126 pad 1: Net-(D113-K) -> Row3
- D126 pad 2: Net-(C9-16-Pin_6) -> Col29
- D127 pad 1: Net-(D113-K) -> Row3
- D127 pad 2: Net-(C9-16-Pin_7) -> Col30
- D128 pad 1: Net-(D113-K) -> Row3
- D128 pad 2: Net-(C9-16-Pin_8) -> Col31
- D13 pad 1: Net-(D1-K) -> Row0
- D13 pad 2: Net-(C9-16-Pin_5) -> Col12
- D14 pad 1: Net-(D1-K) -> Row0
- D14 pad 2: Net-(C9-16-Pin_6) -> Col13
- D15 pad 1: Net-(D1-K) -> Row0
- D15 pad 2: Net-(C9-16-Pin_7) -> Col14
- D16 pad 1: Net-(D1-K) -> Row0
- D16 pad 2: Net-(C9-16-Pin_8) -> Col15
- D17 pad 1: Net-(D17-K) -> Row0
- D17 pad 2: Net-(C1-8-Pin_1) -> Col16
- D18 pad 1: Net-(D17-K) -> Row0
- D18 pad 2: Net-(C1-8-Pin_2) -> Col17
- D19 pad 1: Net-(D17-K) -> Row0
- D19 pad 2: Net-(C1-8-Pin_3) -> Col18
- D2 pad 1: Net-(D1-K) -> Row0
- D2 pad 2: Net-(C1-8-Pin_2) -> Col1
- D20 pad 1: Net-(D17-K) -> Row0
- D20 pad 2: Net-(C1-8-Pin_4) -> Col19
- D21 pad 1: Net-(D17-K) -> Row0
- D21 pad 2: Net-(C1-8-Pin_5) -> Col20
- D22 pad 1: Net-(D17-K) -> Row0
- D22 pad 2: Net-(C1-8-Pin_6) -> Col21
- D23 pad 1: Net-(D17-K) -> Row0
- D23 pad 2: Net-(C1-8-Pin_7) -> Col22
- D24 pad 1: Net-(D17-K) -> Row0
- D24 pad 2: Net-(C1-8-Pin_8) -> Col23
- D25 pad 1: Net-(D17-K) -> Row0
- D25 pad 2: Net-(C9-16-Pin_1) -> Col24
- D26 pad 1: Net-(D17-K) -> Row0
- D26 pad 2: Net-(C9-16-Pin_2) -> Col25
- D27 pad 1: Net-(D17-K) -> Row0
- D27 pad 2: Net-(C9-16-Pin_3) -> Col26
- D28 pad 1: Net-(D17-K) -> Row0
- D28 pad 2: Net-(C9-16-Pin_4) -> Col27
- D29 pad 1: Net-(D17-K) -> Row0
- D29 pad 2: Net-(C9-16-Pin_5) -> Col28
- D3 pad 1: Net-(D1-K) -> Row0
- D3 pad 2: Net-(C1-8-Pin_3) -> Col2
- D30 pad 1: Net-(D17-K) -> Row0
- D30 pad 2: Net-(C9-16-Pin_6) -> Col29
- D31 pad 1: Net-(D17-K) -> Row0
- D31 pad 2: Net-(C9-16-Pin_7) -> Col30
- D32 pad 1: Net-(D17-K) -> Row0
- D32 pad 2: Net-(C9-16-Pin_8) -> Col31
- D33 pad 1: Net-(D33-K) -> Row1
- D33 pad 2: Net-(C1-8-Pin_1) -> Col0
- D34 pad 1: Net-(D33-K) -> Row1
- D34 pad 2: Net-(C1-8-Pin_2) -> Col1
- D35 pad 1: Net-(D33-K) -> Row1
- D35 pad 2: Net-(C1-8-Pin_3) -> Col2
- D36 pad 1: Net-(D33-K) -> Row1
- D36 pad 2: Net-(C1-8-Pin_4) -> Col3
- D37 pad 1: Net-(D33-K) -> Row1
- D37 pad 2: Net-(C1-8-Pin_5) -> Col4
- D38 pad 1: Net-(D33-K) -> Row1
- D38 pad 2: Net-(C1-8-Pin_6) -> Col5
- D39 pad 1: Net-(D33-K) -> Row1
- D39 pad 2: Net-(C1-8-Pin_7) -> Col6
- D4 pad 1: Net-(D1-K) -> Row0
- D4 pad 2: Net-(C1-8-Pin_4) -> Col3
- D40 pad 1: Net-(D33-K) -> Row1
- D40 pad 2: Net-(C1-8-Pin_8) -> Col7
- D41 pad 1: Net-(D33-K) -> Row1
- D41 pad 2: Net-(C9-16-Pin_1) -> Col8
- D42 pad 1: Net-(D33-K) -> Row1
- D42 pad 2: Net-(C9-16-Pin_2) -> Col9
- D43 pad 1: Net-(D33-K) -> Row1
- D43 pad 2: Net-(C9-16-Pin_3) -> Col10
- D44 pad 1: Net-(D33-K) -> Row1
- D44 pad 2: Net-(C9-16-Pin_4) -> Col11
- D45 pad 1: Net-(D33-K) -> Row1
- D45 pad 2: Net-(C9-16-Pin_5) -> Col12
- D46 pad 1: Net-(D33-K) -> Row1
- D46 pad 2: Net-(C9-16-Pin_6) -> Col13
- D47 pad 1: Net-(D33-K) -> Row1
- D47 pad 2: Net-(C9-16-Pin_7) -> Col14
- D48 pad 1: Net-(D33-K) -> Row1
- D48 pad 2: Net-(C9-16-Pin_8) -> Col15
- D49 pad 1: Net-(D49-K) -> Row1
- D49 pad 2: Net-(C1-8-Pin_1) -> Col16
- D5 pad 1: Net-(D1-K) -> Row0
- D5 pad 2: Net-(C1-8-Pin_5) -> Col4
- D50 pad 1: Net-(D49-K) -> Row1
- D50 pad 2: Net-(C1-8-Pin_2) -> Col17
- D51 pad 1: Net-(D49-K) -> Row1
- D51 pad 2: Net-(C1-8-Pin_3) -> Col18
- D52 pad 1: Net-(D49-K) -> Row1
- D52 pad 2: Net-(C1-8-Pin_4) -> Col19
- D53 pad 1: Net-(D49-K) -> Row1
- D53 pad 2: Net-(C1-8-Pin_5) -> Col20
- D54 pad 1: Net-(D49-K) -> Row1
- D54 pad 2: Net-(C1-8-Pin_6) -> Col21
- D55 pad 1: Net-(D49-K) -> Row1
- D55 pad 2: Net-(C1-8-Pin_7) -> Col22
- D56 pad 1: Net-(D49-K) -> Row1
- D56 pad 2: Net-(C1-8-Pin_8) -> Col23
- D57 pad 1: Net-(D49-K) -> Row1
- D57 pad 2: Net-(C9-16-Pin_1) -> Col24
- D58 pad 1: Net-(D49-K) -> Row1
- D58 pad 2: Net-(C9-16-Pin_2) -> Col25
- D59 pad 1: Net-(D49-K) -> Row1
- D59 pad 2: Net-(C9-16-Pin_3) -> Col26
- D6 pad 1: Net-(D1-K) -> Row0
- D6 pad 2: Net-(C1-8-Pin_6) -> Col5
- D60 pad 1: Net-(D49-K) -> Row1
- D60 pad 2: Net-(C9-16-Pin_4) -> Col27
- D61 pad 1: Net-(D49-K) -> Row1
- D61 pad 2: Net-(C9-16-Pin_5) -> Col28
- D62 pad 1: Net-(D49-K) -> Row1
- D62 pad 2: Net-(C9-16-Pin_6) -> Col29
- D63 pad 1: Net-(D49-K) -> Row1
- D63 pad 2: Net-(C9-16-Pin_7) -> Col30
- D64 pad 1: Net-(D49-K) -> Row1
- D64 pad 2: Net-(C9-16-Pin_8) -> Col31
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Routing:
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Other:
- board size 127 x 76.2 mm -> 98.5 x 61.5 mm
- board text removed: "8 x 16 LED Matrix Robert Conde Ver. 1.0"
- board text removed: "HIGH"
- board text removed: "LOW"
